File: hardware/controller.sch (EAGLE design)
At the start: 21 parts, among them IC1 MEGA644, Q1 8MHz, X1 SEGA_JOYPAD, X2 MATRIX1, X3 POWER

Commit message: Updated Hardware
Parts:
- added R2, R3: 470k, resistor:R-EU_0207/10
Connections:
- new net +3V3: R2.2, R3.1, SV2.15, SV2.2
- new net DATA_HIGH: IC1.(TDO/PCINT20)PC4, SV2.13
- new net DATA_LOW: IC1.(TMS/PCINT19)PC3, SV2.18
- new net OE: IC1.(TDI/PCINT21)PC5, SV2.11, SV2.9
- new net RCK: IC1.(TOSC2/PCINT23)PC7, SV2.1
- new net SRCK: IC1.(TOSC1/PCINT22)PC6, SV2.3
- net GND: now also R3.2, SV2.4
- net VCC: now also R2.1, SV2.14, SV2.19, SV2.20
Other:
- moved on the sheet: SV2

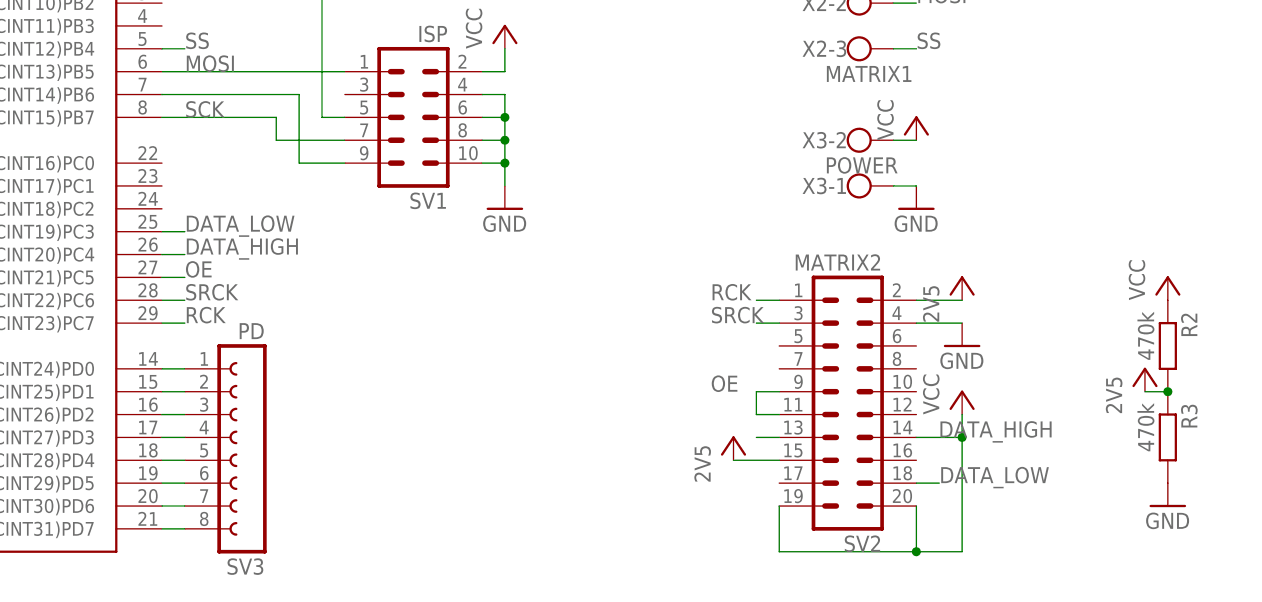
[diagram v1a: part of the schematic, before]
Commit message: Big text marquee and slight hardware modification
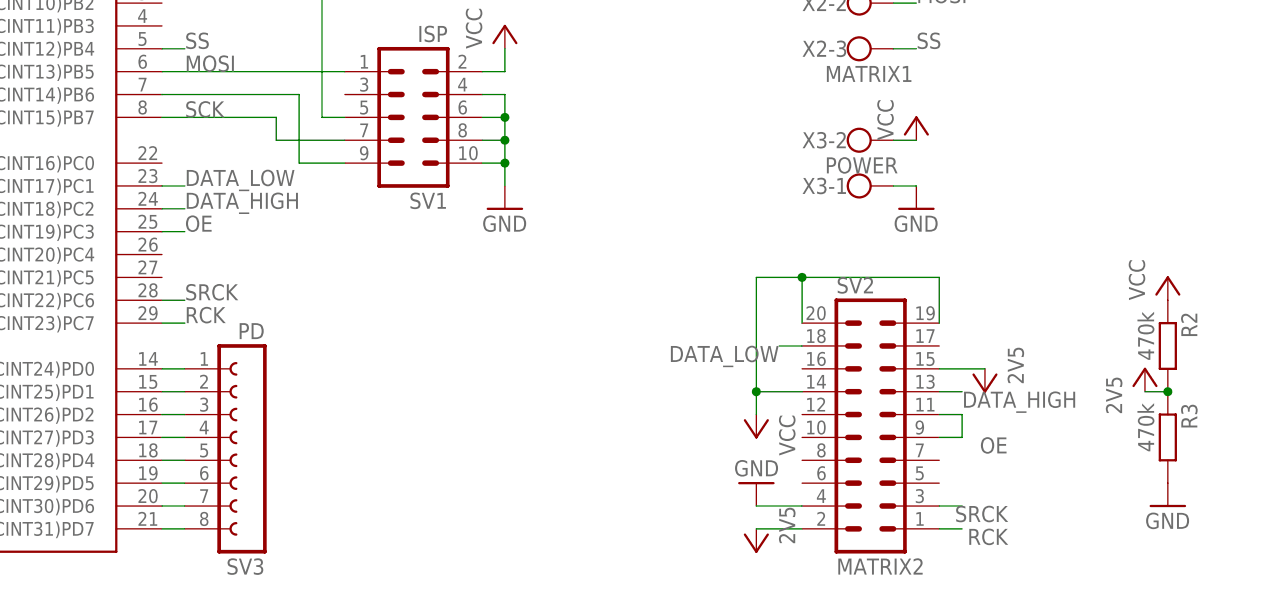
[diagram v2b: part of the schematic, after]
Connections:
- net DATA_HIGH: no longer IC1.(TDO/PCINT20)PC4
- net DATA_LOW: no longer IC1.(TMS/PCINT19)PC3
- net OE: no longer IC1.(TDI/PCINT21)PC5
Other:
- moved on the sheet: SV2
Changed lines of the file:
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@@
 <instance part="P+3" gate="VCC" x="195.58" y="111.76"/>
 <instance part="GND3" gate="1" x="223.52" y="86.36"/>
-<instance part="SV2" gate="1" x="162.56" y="25.4" rot="R180"/>
+<instance part="SV2" gate="1" x="165.1" y="25.4"/>
 <instance part="X2" gate="-1" x="162.56" y="76.2"/>
 <instance part="X2" gate="-2" x="162.56" y="71.12"/>
@@
 <instance part="P+6" gate="VCC" x="198.12" y="40.64"/>
 <instance part="GND8" gate="1" x="198.12" y="15.24"/>
-<instance part="GND9" gate="1" x="175.26" y="33.02"/>
-<instance part="2V5" gate="G$1" x="175.26" y="40.64"/>
+<instance part="GND9" gate="1" x="152.4" y="17.78" rot="R180"/>
+<instance part="2V5" gate="G$1" x="152.4" y="10.16" rot="R180"/>
 <instance part="2V1" gate="G$1" x="195.58" y="30.48"/>
-<instance part="2V2" gate="G$1" x="149.86" y="22.86"/>
-<instance part="P+7" gate="VCC" x="175.26" y="27.94"/>
+<instance part="2V2" gate="G$1" x="177.8" y="27.94" rot="R180"/>
+<instance part="P+7" gate="VCC" x="152.4" y="22.86" rot="R180"/>
 </instances>
 <busses>
@@
 <pinref part="GND9" gate="1" pin="GND"/>
 <pinref part="SV2" gate="1" pin="4"/>
-<wire x1="170.18" y1="35.56" x2="175.26" y2="35.56" width="0.1524" layer="91"/>
+<wire x1="157.48" y1="15.24" x2="152.4" y2="15.24" width="0.1524" layer="91"/>
 </segment>
 <segment>
@@
 <segment>
 <pinref part="SV2" gate="1" pin="20"/>
-<wire x1="170.18" y1="15.24" x2="170.18" y2="10.16" width="0.1524" layer="91"/>
+<wire x1="157.48" y1="35.56" x2="157.48" y2="40.64" width="0.1524" layer="91"/>
 <pinref part="SV2" gate="1" pin="19"/>
-<wire x1="170.18" y1="10.16" x2="154.94" y2="10.16" width="0.1524" layer="91"/>
-<wire x1="154.94" y1="10.16" x2="154.94" y2="15.24" width="0.1524" layer="91"/>
-<wire x1="170.18" y1="10.16" x2="175.26" y2="10.16" width="0.1524" layer="91"/>
-<wire x1="175.26" y1="10.16" x2="175.26" y2="22.86" width="0.1524" layer="91"/>
+<wire x1="157.48" y1="40.64" x2="172.72" y2="40.64" width="0.1524" layer="91"/>
+<wire x1="172.72" y1="40.64" x2="172.72" y2="35.56" width="0.1524" layer="91"/>
+<wire x1="157.48" y1="40.64" x2="152.4" y2="40.64" width="0.1524" layer="91"/>
+<wire x1="152.4" y1="40.64" x2="152.4" y2="27.94" width="0.1524" layer="91"/>
 <pinref part="SV2" gate="1" pin="14"/>
-<wire x1="175.26" y1="25.4" x2="175.26" y2="22.86" width="0.1524" layer="91"/>
-<wire x1="175.26" y1="22.86" x2="170.18" y2="22.86" width="0.1524" layer="91"/>
-<junction x="170.18" y="10.16"/>
+<wire x1="152.4" y1="25.4" x2="152.4" y2="27.94" width="0.1524" layer="91"/>
+<wire x1="152.4" y1="27.94" x2="157.48" y2="27.94" width="0.1524" layer="91"/>
+<junction x="157.48" y="40.64"/>
 <pinref part="P+7" gate="VCC" pin="VCC"/>
-<junction x="175.26" y="22.86"/>
+<junction x="152.4" y="27.94"/>
 </segment>
 </net>
@@
 <segment>
 <pinref part="SV2" gate="1" pin="1"/>
-<wire x1="154.94" y1="38.1" x2="152.4" y2="38.1" width="0.1524" layer="91"/>
-<label x="147.32" y="38.1" size="1.778" layer="95"/>
+<wire x1="172.72" y1="12.7" x2="175.26" y2="12.7" width="0.1524" layer="91"/>
+<label x="180.34" y="12.7" size="1.778" layer="95" rot="R180"/>
 </segment>
 <segment>
@@
 <segment>
 <pinref part="SV2" gate="1" pin="3"/>
-<wire x1="154.94" y1="35.56" x2="152.4" y2="35.56" width="0.1524" layer="91"/>
-<label x="147.32" y="35.56" size="1.778" layer="95"/>
+<wire x1="172.72" y1="15.24" x2="175.26" y2="15.24" width="0.1524" layer="91"/>
+<label x="180.34" y="15.24" size="1.778" layer="95" rot="R180"/>
 </segment>
 <segment>
@@
 <segment>
 <pinref part="SV2" gate="1" pin="11"/>
-<wire x1="154.94" y1="25.4" x2="152.4" y2="25.4" width="0.1524" layer="91"/>
-<wire x1="152.4" y1="25.4" x2="152.4" y2="27.94" width="0.1524" layer="91"/>
+<wire x1="172.72" y1="25.4" x2="175.26" y2="25.4" width="0.1524" layer="91"/>
+<wire x1="175.26" y1="25.4" x2="175.26" y2="22.86" width="0.1524" layer="91"/>
 <pinref part="SV2" gate="1" pin="9"/>
-<wire x1="154.94" y1="27.94" x2="152.4" y2="27.94" width="0.1524" layer="91"/>
-<label x="147.32" y="27.94" size="1.778" layer="95"/>
-</segment>
-<segment>
-<pinref part="IC1" gate="G$1" pin="(TDI/PCINT21)PC5"/>
-<wire x1="86.36" y1="40.64" x2="88.9" y2="40.64" width="0.1524" layer="91"/>
-<label x="88.9" y="40.64" size="1.778" layer="95"/>
+<wire x1="172.72" y1="22.86" x2="175.26" y2="22.86" width="0.1524" layer="91"/>
+<label x="180.34" y="22.86" size="1.778" layer="95" rot="R180"/>
+</segment>
+<segment>
+<label x="88.9" y="45.72" size="1.778" layer="95"/>
+<wire x1="88.9" y1="45.72" x2="86.36" y2="45.72" width="0.1524" layer="91"/>
 </segment>
 </net>
@@
 <segment>
 <pinref part="SV2" gate="1" pin="13"/>
-<wire x1="154.94" y1="22.86" x2="152.4" y2="22.86" width="0.1524" layer="91"/>
-<label x="185.42" y="22.86" size="1.778" layer="95" rot="MR0"/>
-</segment>
-<segment>
-<pinref part="IC1" gate="G$1" pin="(TDO/PCINT20)PC4"/>
-<wire x1="86.36" y1="43.18" x2="88.9" y2="43.18" width="0.1524" layer="91"/>
-<label x="88.9" y="43.18" size="1.778" layer="95"/>
+<wire x1="172.72" y1="27.94" x2="175.26" y2="27.94" width="0.1524" layer="91"/>
+<label x="175.26" y="27.94" size="1.778" layer="95" rot="MR180"/>
+</segment>
+<segment>
+<label x="88.9" y="48.26" size="1.778" layer="95"/>
+<wire x1="86.36" y1="48.26" x2="88.9" y2="48.26" width="0.1524" layer="91"/>
 </segment>
 </net>
@@
 <segment>
 <pinref part="SV2" gate="1" pin="18"/>
-<wire x1="170.18" y1="17.78" x2="172.72" y2="17.78" width="0.1524" layer="91"/>
-<label x="172.72" y="17.78" size="1.778" layer="95"/>
-</segment>
-<segment>
-<pinref part="IC1" gate="G$1" pin="(TMS/PCINT19)PC3"/>
-<wire x1="86.36" y1="45.72" x2="88.9" y2="45.72" width="0.1524" layer="91"/>
-<label x="88.9" y="45.72" size="1.778" layer="95"/>
+<wire x1="157.48" y1="33.02" x2="154.94" y2="33.02" width="0.1524" layer="91"/>
+<label x="154.94" y="33.02" size="1.778" layer="95" rot="R180"/>
+</segment>
+<segment>
+<label x="88.9" y="50.8" size="1.778" layer="95"/>
+<wire x1="86.36" y1="50.8" x2="88.9" y2="50.8" width="0.1524" layer="91"/>
 </segment>
 </net>
@@
 <segment>
 <pinref part="SV2" gate="1" pin="15"/>
-<wire x1="154.94" y1="20.32" x2="149.86" y2="20.32" width="0.1524" layer="91"/>
+<wire x1="172.72" y1="30.48" x2="177.8" y2="30.48" width="0.1524" layer="91"/>
 <pinref part="2V2" gate="G$1" pin="+3V3"/>
 </segment>
@@
 <pinref part="SV2" gate="1" pin="2"/>
 <pinref part="2V5" gate="G$1" pin="+3V3"/>
-<wire x1="175.26" y1="38.1" x2="170.18" y2="38.1" width="0.1524" layer="91"/>
-</segment>
-</net>
+<wire x1="152.4" y1="12.7" x2="157.48" y2="12.7" width="0.1524" layer="91"/>
+</segment>
+</net>
